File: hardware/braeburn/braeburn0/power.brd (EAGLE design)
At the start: 100.5 x 80 mm, 52 parts, among them IC1 7812TV, IC2 7805TV, IC3 7805TV, IC4 ATMEGA48/88/168-AU

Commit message: fixed my fail on use of a zdiode (thanks to samuel), and stuff
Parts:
- added JP1: (no value), jumper:JP1
- added R6: (no value), resistor:R0805
- renumbered R5 to 0OHM
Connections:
- new net N$27: C19.1, C20.1, IC4.4, IC4.6, JP1.1, L7.2, R6.1, SV1.2
- net GND: now also D5.A
- net N$14: now also IC4.29, R6.2, SV1.5; no longer C11.1, D5.A, L3.1
- net N$4: now also C11.1, L3.1
- net N$9: now also JP1.2; no longer C19.1, C20.1, IC4.29, IC4.4, IC4.6, L7.2, SV1.2, SV1.5
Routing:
- net N$14: track 15.2 -> 74.7 mm
- net N$9: track 49.9 -> 4.84 mm
- net N$27: track 0.00 -> 43.0 mm
- net N$4: track 12.7 -> 28.0 mm

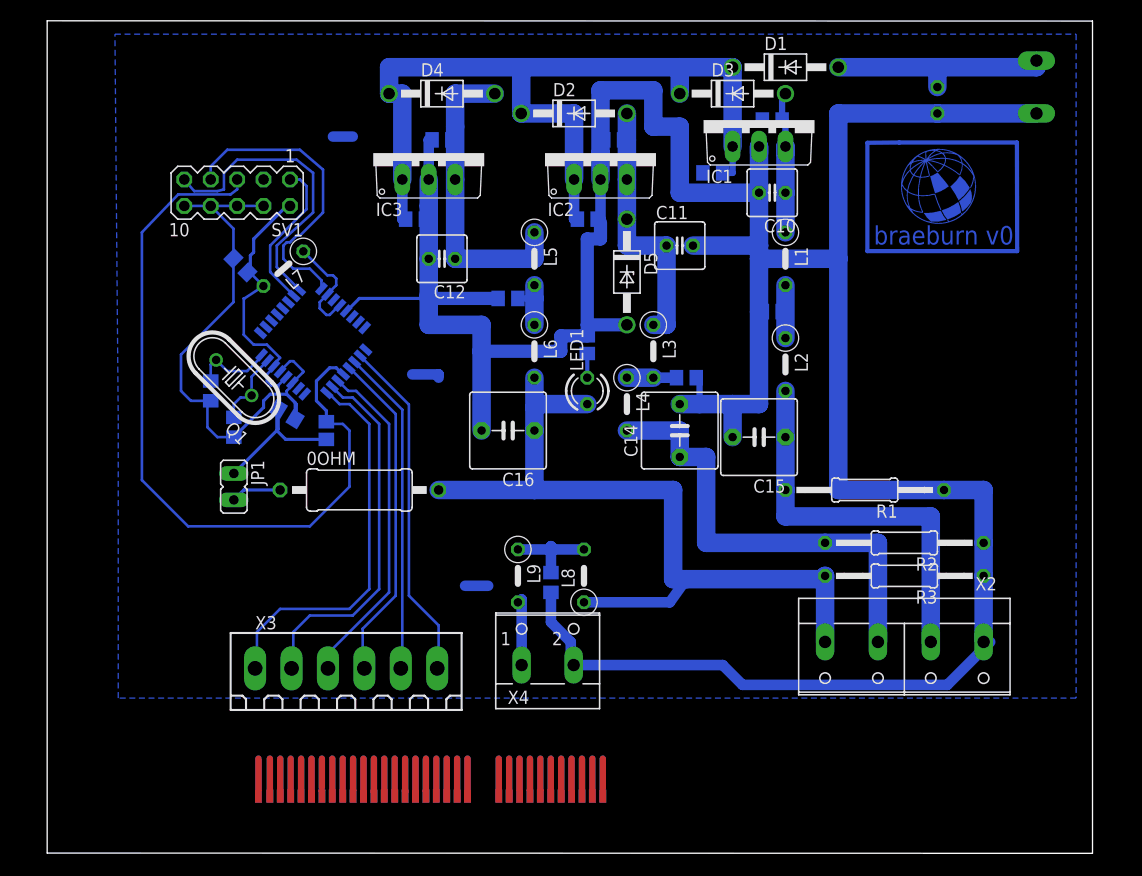
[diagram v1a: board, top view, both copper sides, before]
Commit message: new version of braeburn for new board_port_connector
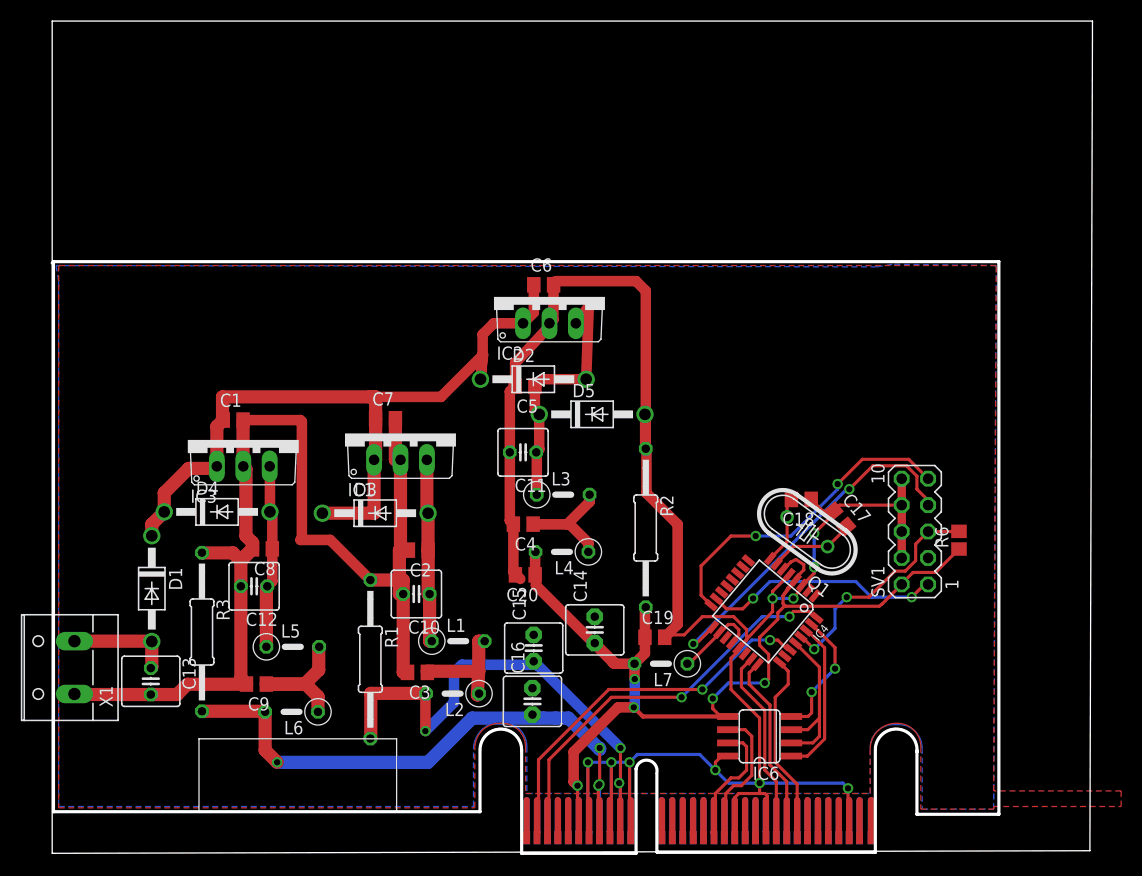
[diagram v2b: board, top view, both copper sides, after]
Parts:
- removed 0OHM: (no value), rcl:0411/15
- removed C21: (no value), rcl:C0805
- removed JP1: (no value), jumper:JP1
- removed L8, L9: (no value), rcl:0207/5V
- removed LED1: (no value), led:LED3MM
- removed R4: (no value), rcl:R2012
- removed X2: (no value), con-wago-508:W237-4P
- removed X3: (no value), con-weidmueller-sl35:180G-6
- removed X4: (no value), con-wago-500:W237-102
- added IC6: MAX481CSA, maxim:SO08
- added U$2: HGG_LOGO, hgg:HGG_LOGO
- C14, C15, C16: device capacitor-wima:C5B7.2 -> capacitor-wima:C2.5-6
- U$1: value FRIENDSHIPEDGECONNECTOR -> FRIENDSHIPCONNECTOR
- moved X1 109.1 mm to (1.50, 17.9), flipped to the top
- moved U$1 98.4 mm to (0.11, 16.0), flipped to the top
- moved C13 94.0 mm to (9.48, 16.5), flipped to the top
- moved D1 78.9 mm to (9.57, 25.4), turned to 270 degrees
- moved SV1 72.8 mm to (82.9, 30.9), turned to 90 degrees
- moved R3 67.7 mm to (14.4, 21.3), turned to 270 degrees
- moved R6 61.7 mm to (87.2, 30.1), flipped to the top
- moved C17 58.9 mm to (75.7, 32.1), flipped to the top, turned to 310.2 degrees
- moved C18 57.7 mm to (72.0, 34.0), flipped to the top, turned to 180 degrees
- moved Q1 57.1 mm to (72.6, 30.9), turned to 143.8 degrees
- moved C2 53.5 mm to (35.2, 29.1), flipped to the top, turned to 180 degrees
- moved C19 53.5 mm to (57.9, 20.8), flipped to the top, turned to 0 degrees
- moved D3 53.0 mm to (31.1, 32.7)
- moved L7 52.5 mm to (58.5, 18.2), turned to 180 degrees
- moved C1 51.9 mm to (17.4, 41.6), flipped to the top
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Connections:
- removed net N$10: C14.1, L4.2, R2.2, X2.3
- removed net N$11: 0OHM.2, C16.1, L6.2, L8.1, LED1.A, R3.2, X2.4
- removed net N$19: LED1.K, R4.1
- removed net N$21: IC4.31, X3.2
- removed net N$22: IC4.30, X3.3
- removed net N$23: IC4.28, X3.4
- removed net N$24: IC4.27, X3.5
- removed net N$25: IC4.26, X3.6
- removed net N$27: C19.1, C20.1, IC4.4, IC4.6, JP1.1, L7.2, R6.1, SV1.2
- removed net N$28: C15.1, L2.2, R1.2, X2.2
- removed net N$29: C21.2, L8.2, L9.1
- removed net N$30: L9.2, X4.1
- removed net N$9: 0OHM.1, JP1.2
- new net +12V: C15.1, L2.2, R1.2, U$1.A10(+12V), U$1.B10(+12V)
- new net +3V3: C14.1, C19.1, C20.1, IC4.4, IC4.6, IC6.5, L4.2, L7.2, R2.2, R6.1, SV1.2, U$1.A06(+3V3), U$1.B06(+3V3)
- new net +5V: C16.1, L6.2, R3.2, U$1.A08(+5V), U$1.B08(+5V)
- new net BUS0+: IC6.6, U$1.A18(BUS0+)
- new net BUS0-: IC6.7, U$1.A17(BUS0-)
- new net BUSCTL: IC4.28, IC6.2, IC6.3
- new net CS: IC4.32, U$1.A03(/CS,IRQ)
- new net IRQ: IC4.27, U$1.A02(IRQ)
- new net N$34: U$1.A01(PRSNT1), U$1.A32(PRSNT2)
- new net RX: IC4.30, IC6.1
- new net SLOWTIMECLK: IC4.24, U$1.A24(SLOWCLKCLK)
- new net SLOWTIMECS: IC4.25, U$1.A25(SLOWCLK/CS)
- new net SLOWTIMEMOSI: IC4.23, U$1.A23(SLOWTIMEMOSI)
- new net TX: IC4.31, IC6.4
- net GND: now also IC6.8, U$1.A07(GND), U$1.A09(GND), U$1.A11(GND), U$1.A19(GND), U$1.A22(GND), U$1.A30(GND), U$1.B07(GND), U$1.B09(GND), U$1.B11(GND); no longer C21.1, R4.2, X2.1, X4.2
- net N$20: now also U$1.A13(TDO), U$1.A14(TMS); no longer IC4.32, X3.1
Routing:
- net +3V3: track 0.00 -> 105.0 mm, vias 0 -> 5
- net N$11: track 79.2 -> 0.00 mm
- net +5V: track 0.00 -> 61.7 mm, vias 0 -> 4
- net +12V: track 0.00 -> 54.6 mm, vias 0 -> 3
- net N$14: track 74.7 -> 22.4 mm, vias 0 -> 2
- net N$26: track 49.6 -> 0.00 mm
- net N$10: track 44.5 -> 0.00 mm
- net N$27: track 43.0 -> 0.00 mm
- net CS: track 0.00 -> 39.5 mm, vias 0 -> 2
- net N$28: track 38.1 -> 0.00 mm
- net N$20: track 37.3 -> 0.00 mm
- net IRQ: track 0.00 -> 36.9 mm, vias 0 -> 2
- net GND: track 375.4 -> 338.7 mm, vias 0 -> 10
- net N$21: track 35.4 -> 0.00 mm
- net N$25: track 33.2 -> 0.00 mm
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- added copper zone on layer 1, net GND
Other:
- board size 100.5 x 80 mm -> 100 x 80 mm
- board text removed: "braeburn v0"

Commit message: design rules
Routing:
- net N$34: track 0.00 -> 20.2 mm, vias 0 -> 2
- net N$20: track 0.00 -> 9.13 mm
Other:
- outline, holes or cut-outs redrawn

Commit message: current status
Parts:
- added IC5, IC7: LM741D, linear:SO08
- moved IC1 9.38 mm to (33.2, 49.7)
- moved R6 9.34 mm to (82.8, 38.4), turned to 180 degrees
- moved IC3 8.50 mm to (18.1, 48.2)
- moved C1 8.26 mm to (17.0, 49.9)
- moved C7 8.25 mm to (32.3, 50.0)
- moved R1 1.00 mm to (31.6, 18.6)
- moved C3 0.75 mm to (35.1, 18.1)
- moved C4 0.62 mm to (45.3, 31.0)
- moved D2 0.18 mm to (46.4, 45.7)
- turned SV1 to 270 degrees
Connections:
- new net 3V3A: C11.1, C5.1, D2.A, D5.C, IC2.3, IC5.3, L3.1
- new net 3V3B: C4.1, IC5.2, L3.2, L4.1
- new net 3V3METER: IC4.19, IC5.6
- new net 5VA: C12.1, C8.1, D4.A, IC3.3, IC7.3, L5.1
- new net 5VB: C9.1, IC7.2, L5.2, L6.1
- new net 5VMETER: IC4.22, IC7.6
- net GND: now also IC5.1, IC5.4, IC5.5, IC7.1, IC7.4, IC7.5, U$1.A27(GND)
- net N$3: now also IC7.7; no longer C12.1, C8.1, D4.A, IC3.3, L5.1
- net N$4: now also IC7.8; no longer C11.1, C5.1, D2.A, D5.C, IC2.3, L3.1
- net N$6: now also IC5.7; no longer C9.1, L5.2, L6.1
- net N$7: now also IC5.8; no longer C4.1, L3.2, L4.1
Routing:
- net GND: track 338.8 -> 519.7 mm, vias 10 -> 8
- net 5VMETER: track 0.00 -> 46.6 mm, vias 0 -> 2
- net 3V3METER: track 0.00 -> 34.6 mm
- net 5VA: track 0.00 -> 29.6 mm
- net 3V3B: track 0.00 -> 28.9 mm
- net 3V3A: track 0.00 -> 26.2 mm
- net N$4: track 25.0 -> 0.00 mm
- net 5VB: track 0.00 -> 19.0 mm
- net N$3: track 17.7 -> 0.00 mm
- net N$6: track 14.8 -> 0.00 mm
- net +3V3: track 104.9 -> 118.9 mm, vias 5 -> 7
- net N$1: track 76.5 -> 88.2 mm
- net N$7: track 10.7 -> 0.00 mm
- net N$5: track 17.9 -> 27.4 mm
- net N$14: track 22.4 -> 31.6 mm
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- removed copper zone on layer 1, net GND
- removed copper zone on layer 16, net GND
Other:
- outline, holes or cut-outs redrawn

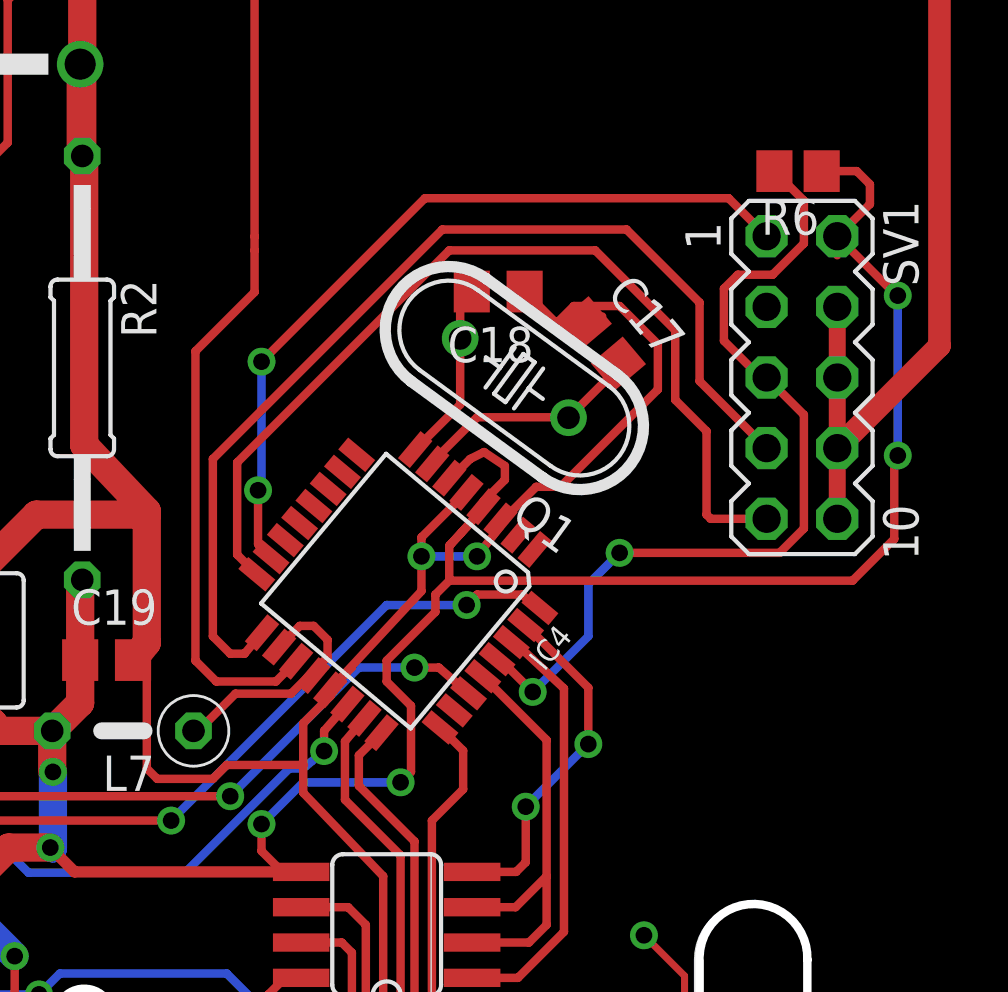
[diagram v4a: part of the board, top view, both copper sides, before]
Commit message: removed vias
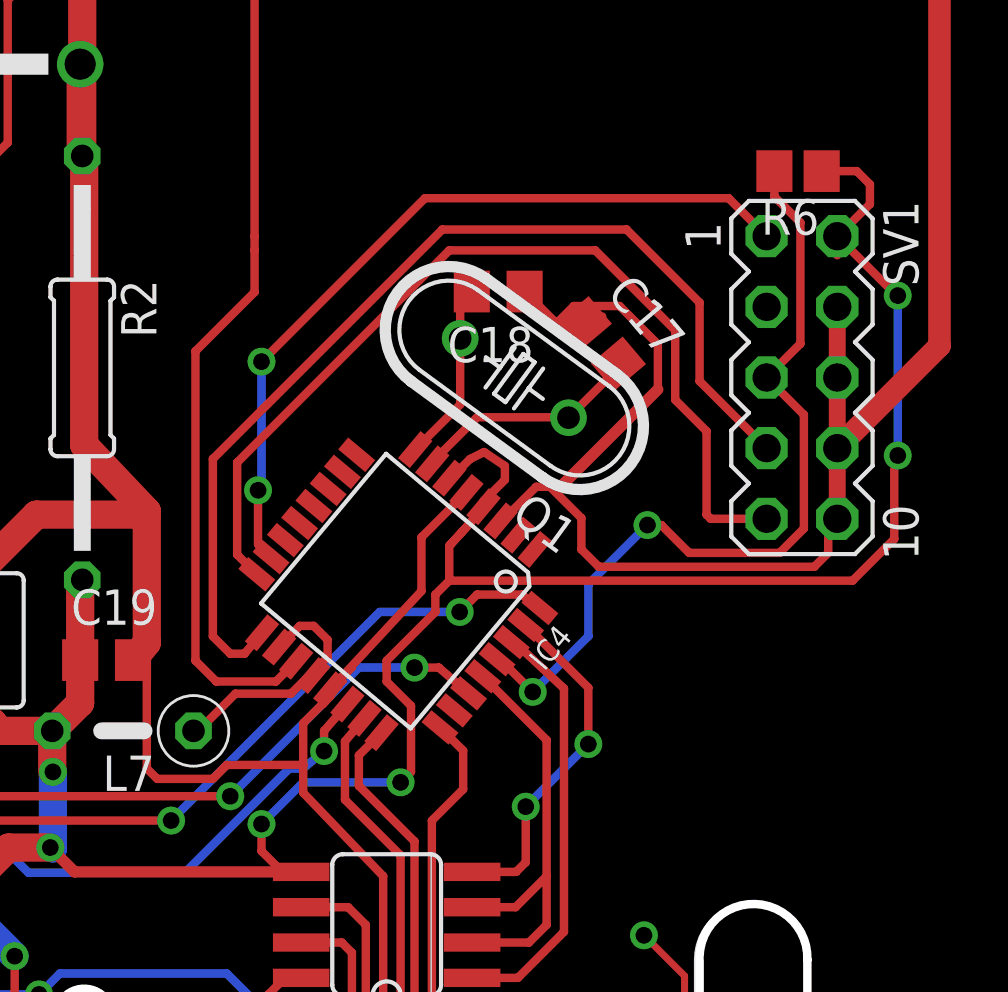
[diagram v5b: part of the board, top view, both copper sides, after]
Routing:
- net GND: track 519.7 -> 529.6 mm, vias 8 -> 6
- net N$14: track 31.6 -> 30.2 mm
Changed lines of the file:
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@@
 <wire x1="65.973378125" y1="19.700284375" x2="65.973378125" y2="19.723378125" width="0.3048" layer="1"/>
 <wire x1="65.973378125" y1="19.723378125" x2="69.25" y2="23.25" width="0.3048" layer="1"/>
-<wire x1="69.25" y1="23.25" x2="69.25" y2="24.5" width="0.3048" layer="1"/>
-<wire x1="69.25" y1="25.18309375" x2="70.86661875" y2="26.7997125" width="0.3048" layer="1"/>
-<wire x1="72.094084375" y1="25.773390625" x2="72.094084375" y2="25.594084375" width="0.3048" layer="1"/>
-<wire x1="72.094084375" y1="25.594084375" x2="71.25" y2="24.5" width="0.3048" layer="1"/>
-<via x="71.25" y="24.5" extent="1-16" drill="0.6"/>
-<wire x1="71.25" y1="24.5" x2="69.25" y2="24.5" width="0.3048" layer="16"/>
-<via x="69.25" y="24.5" extent="1-16" drill="0.6"/>
-<wire x1="69.25" y1="24.5" x2="69.25" y2="25.18309375" width="0.3048" layer="1"/>
 <wire x1="65.973378125" y1="19.700284375" x2="65.973378125" y2="19.473378125" width="0.3048" layer="1"/>
 <wire x1="65.973378125" y1="19.473378125" x2="65.75" y2="19.25" width="0.3048" layer="1"/>
@@
 <wire x1="76.375" y1="33.5" x2="77.75" y2="32.125" width="0.3048" layer="1"/>
 <wire x1="77.75" y1="32.125" x2="77.75" y2="30.5" width="0.3048" layer="1"/>
-<wire x1="77.75" y1="30.5" x2="74.25" y2="27" width="0.3048" layer="1"/>
-<wire x1="74.25" y1="27" x2="73.375" y2="27" width="0.3048" layer="1"/>
-<wire x1="73.375" y1="27" x2="72.148390625" y2="25.773390625" width="0.3048" layer="1"/>
-<wire x1="72.148390625" y1="25.773390625" x2="72.094084375" y2="25.773390625" width="0.3048" layer="1"/>
+<wire x1="74.25" y1="27" x2="73.875" y2="27" width="0.3048" layer="1"/>
 <wire x1="87.875" y1="32.065" x2="84.2" y2="28.39" width="0.8128" layer="1"/>
+<wire x1="74.25" y1="27" x2="77.75" y2="30.5" width="0.4064" layer="1"/>
+<wire x1="69.25" y1="23.25" x2="69.25" y2="25.18309375" width="0.3048" layer="1"/>
+<wire x1="69.25" y1="25.18309375" x2="70.86661875" y2="26.7997125" width="0.3048" layer="1"/>
+<wire x1="72.094084375" y1="25.773390625" x2="72.148390625" y2="25.773390625" width="0.3048" layer="1"/>
+<wire x1="72.148390625" y1="25.773390625" x2="73.375" y2="27" width="0.3048" layer="1"/>
+<wire x1="73.375" y1="27" x2="73.875" y2="27" width="0.3048" layer="1"/>
+<wire x1="73.875" y1="27" x2="75" y2="25.875" width="0.3048" layer="1"/>
+<wire x1="75" y1="25.875" x2="75" y2="24.75" width="0.3048" layer="1"/>
+<wire x1="75" y1="24.75" x2="75.625" y2="24.125" width="0.3048" layer="1"/>
+<wire x1="75.625" y1="24.125" x2="83.375" y2="24.125" width="0.3048" layer="1"/>
+<wire x1="83.375" y1="24.125" x2="83.875" y2="24.625" width="0.3048" layer="1"/>
+<wire x1="83.875" y1="24.625" x2="83.875" y2="25.525" width="0.3048" layer="1"/>
+<wire x1="83.875" y1="25.525" x2="84.2" y2="25.85" width="0.3048" layer="1"/>
 <wire x1="57" y1="42.25" x2="56.98" y2="42.195" width="0" layer="19" extent="1-1"/>
 <wire x1="48.195" y1="54.645" x2="48.375" y2="55" width="0" layer="19" extent="1-1"/>
@@
 <contactref element="R6" pad="2"/>
 <contactref element="SV1" pad="5"/>
-<via x="76.375" y="24.625" extent="1-16" drill="0.6"/>
-<wire x1="76.375" y1="24.625" x2="75.25" y2="23.5" width="0.3048" layer="16"/>
+<via x="77.375" y="25.625" extent="1-16" drill="0.6"/>
+<wire x1="77.375" y1="25.625" x2="75.25" y2="23.5" width="0.3048" layer="16"/>
 <wire x1="75.25" y1="23.5" x2="75.25" y2="21.625" width="0.3048" layer="16"/>
 <wire x1="75.25" y1="21.625" x2="73.25" y2="19.625" width="0.3048" layer="16"/>
@@
 <wire x1="73.25" y1="19.625" x2="72.071621875" y2="20.803378125" width="0.3048" layer="1"/>
 <wire x1="72.071621875" y1="20.803378125" x2="71.9697125" y2="20.803378125" width="0.3048" layer="1"/>
-<wire x1="81.66" y1="31.41" x2="81.66" y2="30.93" width="0" layer="19" extent="1-16"/>
 <wire x1="81.66" y1="30.93" x2="83" y2="29.59" width="0.3048" layer="1"/>
 <wire x1="83" y1="29.59" x2="83" y2="25.5" width="0.3048" layer="1"/>
 <wire x1="83" y1="25.5" x2="82.125" y2="24.625" width="0.3048" layer="1"/>
-<wire x1="82.125" y1="24.625" x2="76.375" y2="24.625" width="0.3048" layer="1"/>
-<wire x1="81.94" y1="38.35" x2="83" y2="37.29" width="0.3048" layer="1"/>
-<wire x1="83" y1="37.29" x2="83" y2="35.75" width="0.3048" layer="1"/>
-<wire x1="83" y1="35.75" x2="81.875" y2="34.625" width="0.3048" layer="1"/>
-<wire x1="81.875" y1="34.625" x2="80.625" y2="34.625" width="0.3048" layer="1"/>
-<wire x1="80.625" y1="34.625" x2="80.125" y2="34.125" width="0.3048" layer="1"/>
-<wire x1="80.125" y1="34.125" x2="80.125" y2="32.25" width="0.3048" layer="1"/>
-<wire x1="80.125" y1="32.25" x2="81.445" y2="30.93" width="0.3048" layer="1"/>
-<wire x1="81.445" y1="30.93" x2="81.66" y2="30.93" width="0.3048" layer="1"/>
+<wire x1="82.125" y1="24.625" x2="78.875" y2="24.625" width="0.3048" layer="1"/>
+<wire x1="78.875" y1="24.625" x2="77.875" y2="25.625" width="0.3048" layer="1"/>
+<wire x1="77.875" y1="25.625" x2="77.375" y2="25.625" width="0.3048" layer="1"/>
+<wire x1="81.66" y1="30.93" x2="82.875" y2="32.145" width="0.3048" layer="1"/>
+<wire x1="82.875" y1="32.145" x2="82.875" y2="36.5" width="0.3048" layer="1"/>
+<wire x1="82.875" y1="36.5" x2="81.94" y2="37.435" width="0.3048" layer="1"/>
+<wire x1="81.94" y1="37.435" x2="81.94" y2="38.35" width="0.3048" layer="1"/>
 </signal>
 <signal name="+5V">
@@
 <wire x1="53.75" y1="15" x2="60.25" y2="15" width="0.3048" layer="1"/>
 <via x="60.25" y="15" extent="1-16" drill="0.6"/>
-<wire x1="60.25" y1="15" x2="68" y2="22.75" width="0.3048" layer="16"/>
-<wire x1="68" y1="22.75" x2="70.875" y2="22.75" width="0.3048" layer="16"/>
-<via x="70.875" y="22.75" extent="1-16" drill="0.6"/>
-<wire x1="70.875" y1="22.75" x2="71.25" y2="23.125" width="0.3048" layer="1"/>
+<wire x1="60.25" y1="15" x2="67.75" y2="22.5" width="0.3048" layer="16"/>
+<wire x1="67.75" y1="22.5" x2="70.625" y2="22.5" width="0.3048" layer="16"/>
+<via x="70.625" y="22.5" extent="1-16" drill="0.6"/>
+<wire x1="70.625" y1="22.5" x2="71.25" y2="23.125" width="0.3048" layer="1"/>
 <wire x1="71.25" y1="23.125" x2="72.875" y2="23.125" width="0.3048" layer="1"/>
 <wire x1="72.875" y1="23.125" x2="73.355425" y2="22.644575" width="0.3048" layer="1"/>
